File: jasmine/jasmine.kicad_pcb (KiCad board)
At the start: 2 copper layers, 70.7 x 53.3 mm, 27 parts, among them J1 NEIGHBOR1, J2 NEIGHBOR2, J3 USB-MICRO-B-SHIELDED, J4 LIPO_BATT_CONN, J7 BONUS_ROW, P1 TEST_POINT, P2 TEST_POINT, P3 TEST_POINT, P5 3.7_VDC, U1 MCP73831T

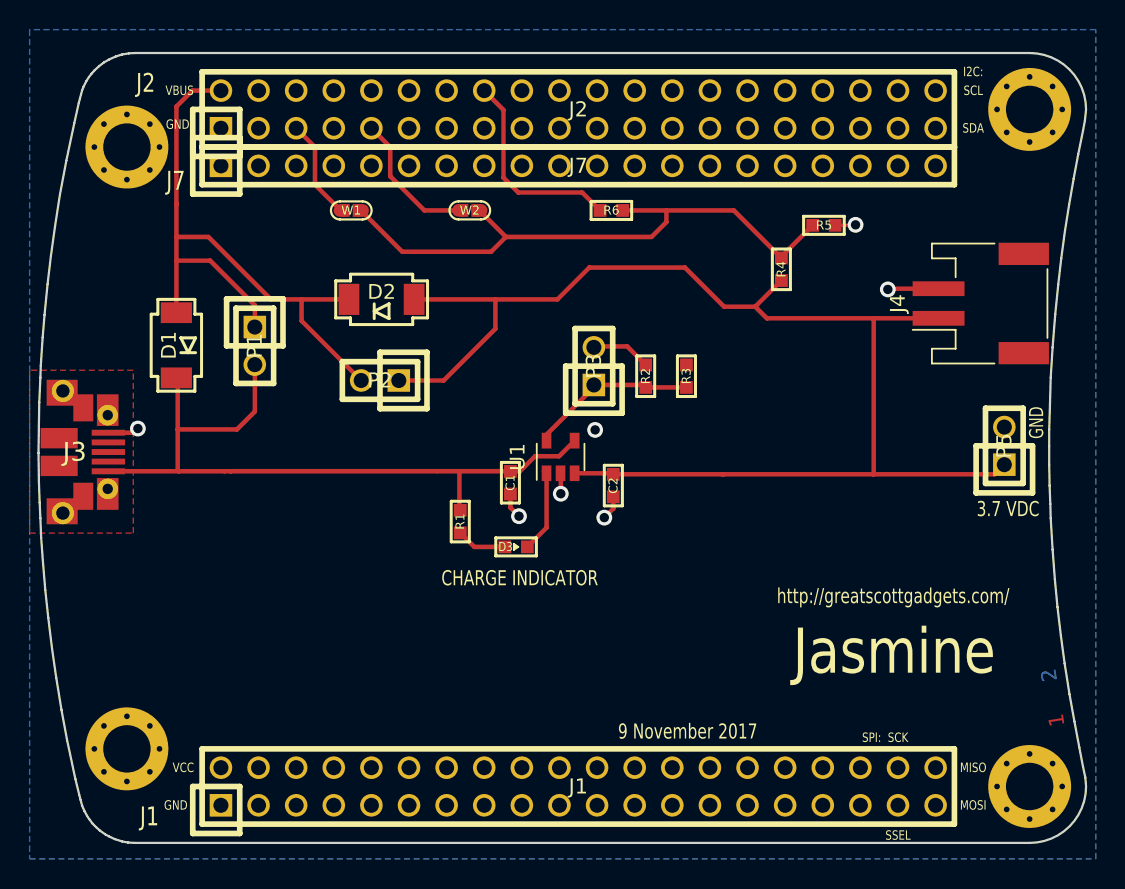
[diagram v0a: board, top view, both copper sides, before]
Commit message: JASMINE: Revised charge rate config; Added DNP JST connector; Added DNP screw terminal; Added load switch w/ LED indicator; Updated labeling on silkscreen LUCKY BAMBOO: updated soldermask clearance
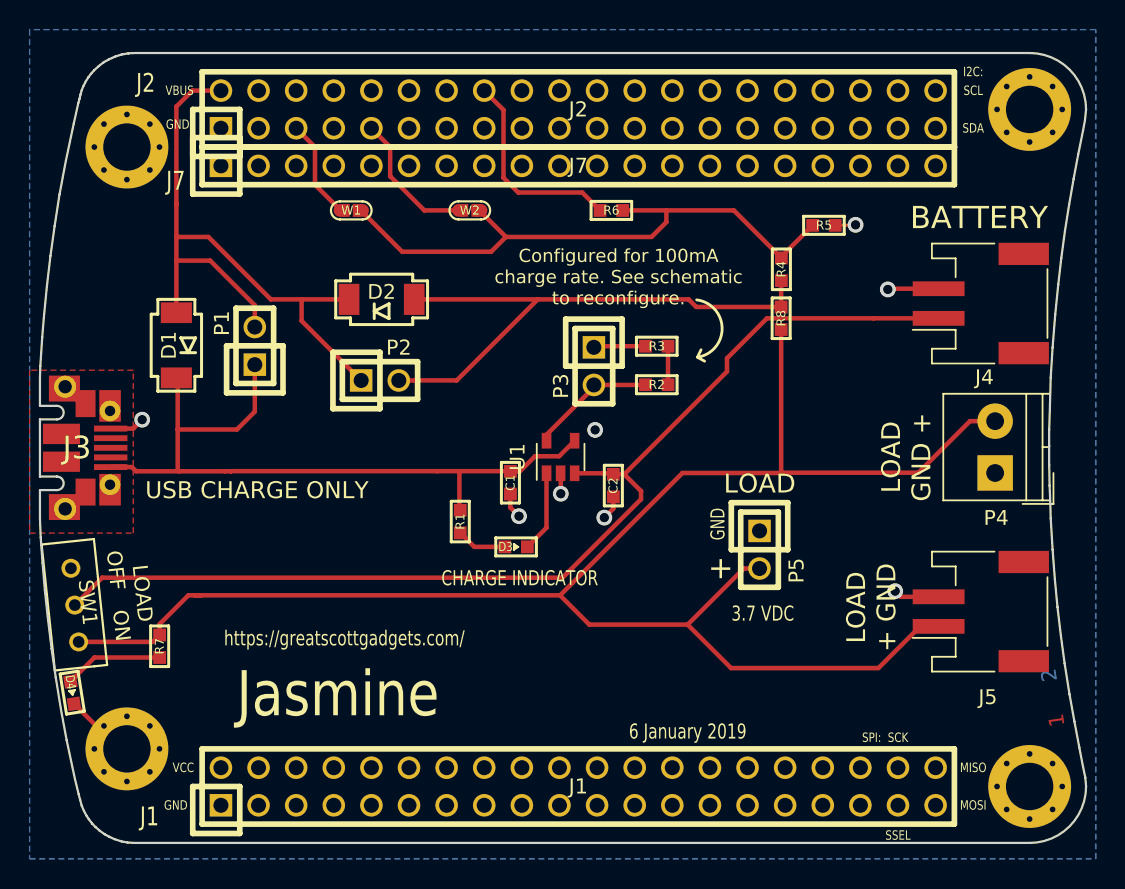
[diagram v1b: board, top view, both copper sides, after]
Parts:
- added D4: LED, gsg-modules:0603D, F.Cu at (111.9, 111.8)
- added J5: 2PIN_BATT_CONN, gsg-modules:JST_PH_S2B-PH-SM4-TB_02x2.00mm_Angled, F.Cu at (173.3, 106.3)
- added P4: 3.7_VDC, gsg-modules:TerminalBlock_4UCON_19963_02x3.5mm_Straight, F.Cu at (174.2, 96.9)
- added R7: 330, gsg-modules:0603, F.Cu at (117.8, 108.6)
- added R8: 0, gsg-modules:0603, F.Cu at (159.8, 86.5)
- added SW1: SW_SPDT, gsg-modules:MHSS1105, F.Cu at (112.0, 105.9)
- J4: footprint Connectors_JST:JST_PH_S2B-PH-SM4-TB_02x2.00mm_Angled -> gsg-modules:JST_PH_S2B-PH-SM4-TB_02x2.00mm_Angled
- R2: value 10k -> 7.5k
- moved P5 18.0 mm to (158.3, 102.1), turned to 270 degrees
- moved R3 2.85 mm to (151.3, 88.4), turned to 0 degrees
- moved R2 0.94 mm to (151.3, 91.0), turned to 180 degrees
- moved J3 0.32 mm to (109.7, 95.2)
- turned P1 to 90 degrees
- turned P2 to 0 degrees
- turned P3 to 270 degrees
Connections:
- D2 pad 2: Net-(C2-Pad2) -> Net-(D2-Pad2)
- P1 pad 1: /+5V -> Net-(C1-Pad2)
- P1 pad 2: Net-(C1-Pad2) -> /+5V
- P2 pad 1: Net-(C2-Pad2) -> /+5V
- P2 pad 2: /+5V -> Net-(D2-Pad2)
- P3 pad 1: Net-(P3-Pad1) -> GND
- P3 pad 2: GND -> Net-(P3-Pad2)
- P5 pad 1: Net-(C2-Pad2) -> GND
- P5 pad 2: GND -> Net-(J5-Pad1)
- R2 pad 1: GND -> Net-(R2-Pad1)
- R2 pad 2: Net-(P3-Pad1) -> Net-(P3-Pad2)
- R3 pad 2: Net-(P3-Pad1) -> Net-(R2-Pad1)
- R4 pad 1: Net-(C2-Pad2) -> Net-(D2-Pad2)
- U1 pad 5: Net-(P3-Pad1) -> Net-(P3-Pad2)
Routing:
- net Net-(J5-Pad1): track 0.00 -> 114.1 mm
- net Net-(D2-Pad2): track 0.00 -> 38.4 mm
- net Net-(C2-Pad2): track 90.5 -> 73.2 mm
- net Net-(P3-Pad1): track 11.4 -> 0.00 mm
- net GND: track 15.7 -> 24.3 mm, vias 6 -> 7
- net Net-(P3-Pad2): track 0.00 -> 8.58 mm
- net Net-(D4-Pad2): track 0.00 -> 6.69 mm
- net Net-(R2-Pad1): track 0.00 -> 2.60 mm
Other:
- board size 70.7 x 53.3 mm -> 70.6 x 53.3 mm
- board text added: "+"
- board text added: "6 January 2019"
- board text added: "BATTERY"
- board text added: "Configured for 100mA charge rate. See schematic to reconfigure."
- board text added: "LOAD"
- board text added: "LOAD + GND"
- board text added: "LOAD GND +"
- board text added: "LOAD OFF ON"
- board text added: "USB CHARGE ONLY"
- board text added: "https://greatscottgadgets.com/"
- board text removed: "9 November 2017"
- board text removed: "http://greatscottgadgets.com/"

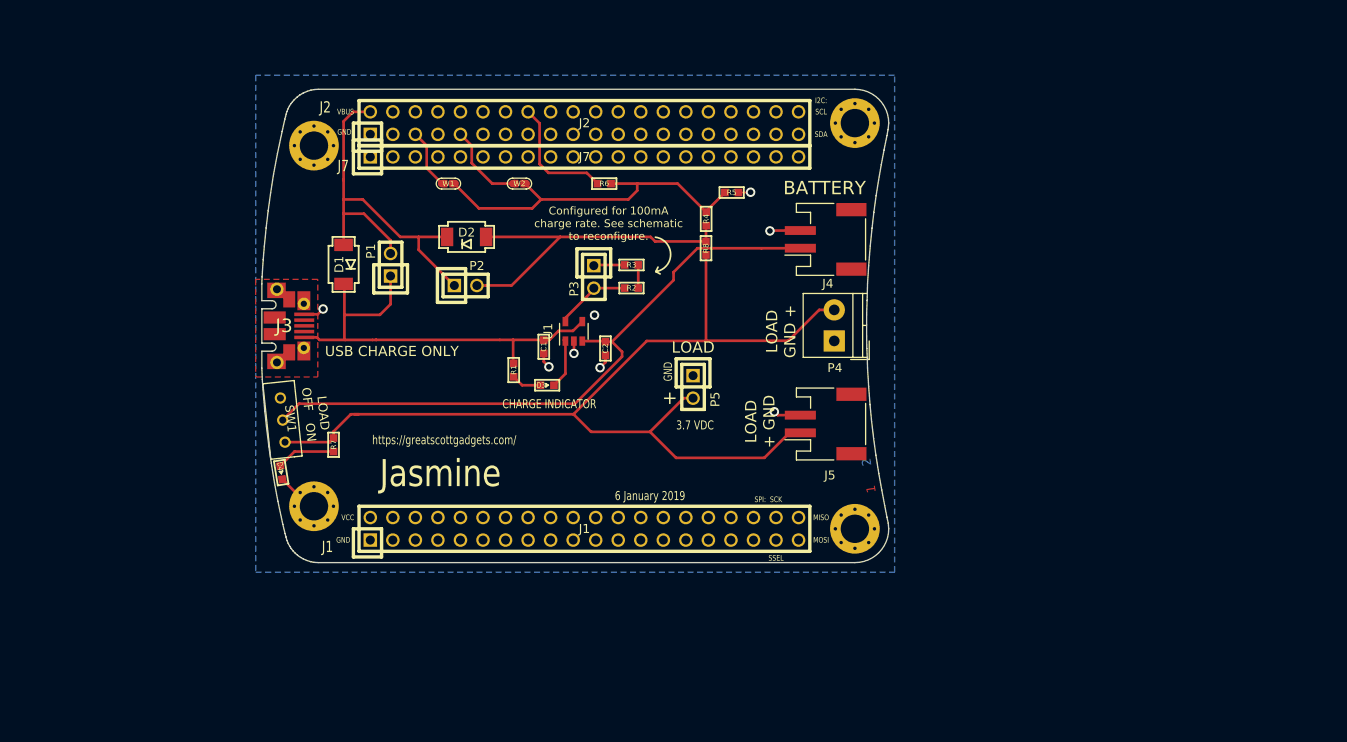
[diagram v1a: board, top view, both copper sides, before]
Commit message: Cleaned up jasmine.sch; Started Jasmine layout
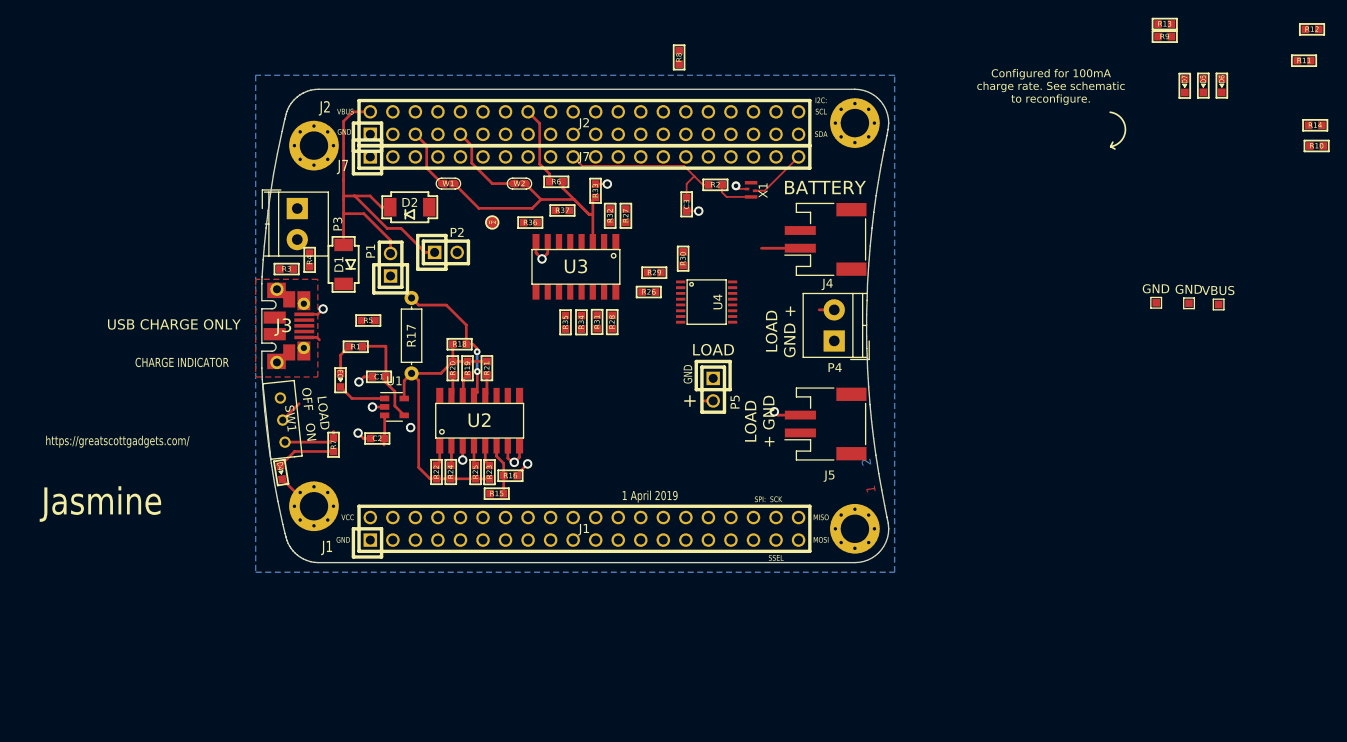
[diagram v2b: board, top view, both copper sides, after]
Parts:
- added C3: C, gsg-modules:0603, F.Cu at (157.6, 81.5)
- added D5: LED, gsg-modules:0603D, F.Cu at (215.8, 68.2)
- added D6: LED, gsg-modules:0603D, F.Cu at (217.9, 68.2)
- added D7: LED, gsg-modules:0603D, F.Cu at (213.7, 68.2)
- added GND: , gsg-modules:1Pin_0603, F.Cu at (210.5, 92.6)
- added GND: , gsg-modules:1Pin_0603, F.Cu at (214.2, 92.7)
- added R10: 330, gsg-modules:0603, F.Cu at (228.6, 75.0)
- added R11: 10k, gsg-modules:0603, F.Cu at (227.1, 65.4)
- added R12: 330, gsg-modules:0603, F.Cu at (228.0, 61.8)
- added R13: 10k, gsg-modules:0603, F.Cu at (211.4, 61.2)
- added R14: 10k, gsg-modules:0603, F.Cu at (228.4, 72.6)
- added R15: 10k, gsg-modules:0603, F.Cu at (136.2, 114.2)
- added R16: 10k, gsg-modules:0603, F.Cu at (137.7, 112.1)
- added R17: R, gsg-modules:RESISTOR-AXIAL-2.3x6.0mm, F.Cu at (126.6, 96.3)
- added R18: 67k, gsg-modules:0603, F.Cu at (132.0, 97.3)
- added R19: 2k, gsg-modules:0603, F.Cu at (132.9, 100.0)
- added R20: 2.5k, gsg-modules:0603, F.Cu at (131.2, 100.0)
- added R21: 3.33k, gsg-modules:0603, F.Cu at (135.1, 100.0)
- added R22: 5k, gsg-modules:0603, F.Cu at (129.4, 111.7)
- added R23: 10k, gsg-modules:0603, F.Cu at (135.3, 111.7)
- added R24: 25k, gsg-modules:0603, F.Cu at (131.0, 111.7)
- added R25: 67k, gsg-modules:0603, F.Cu at (133.8, 111.7)
- added R26: 10k, gsg-modules:0603, F.Cu at (153.3, 91.4)
- added R27: 0, gsg-modules:0603, F.Cu at (150.7, 82.8)
- added R28: 100k, gsg-modules:0603, F.Cu at (149.2, 94.8)
- added R29: 10k, gsg-modules:0603, F.Cu at (153.9, 89.2)
- added R30: 10k, gsg-modules:0603, F.Cu at (157.2, 87.7)
- added R31: 100k, gsg-modules:0603, F.Cu at (147.5, 94.8)
- added R32: 100k, gsg-modules:0603, F.Cu at (148.9, 82.8)
- added R33: 100k, gsg-modules:0603, F.Cu at (147.3, 80.0)
- added R34: 100k, gsg-modules:0603, F.Cu at (145.7, 94.8)
- added R35: 100k, gsg-modules:0603, F.Cu at (143.9, 94.8)
- added R36: 100k, gsg-modules:0603, F.Cu at (139.9, 83.6)
- added R37: 100k, gsg-modules:0603, F.Cu at (143.6, 82.2)
- added R9: 330, gsg-modules:0603, F.Cu at (211.4, 62.7)
- added TP4: TestPoint, gsg-modules:TESTPOINT-50MIL, F.Cu at (135.7, 83.6)
- added U2: 74HC4051, gsg-modules:SOIC16, F.Cu at (134.2, 105.9)
- added U3: 74HC4051, gsg-modules:SOIC16, F.Cu at (145.1, 88.6)
- added U4: PCA9674, gsg-modules:TSSOP16, F.Cu at (159.8, 92.6)
- added VBUS: , gsg-modules:1Pin_0603, F.Cu at (217.5, 92.8)
- added X1: SiT1533, gsg-modules:SiT1533, F.Cu at (164.8, 79.9)
- P3: value TEST_POINT -> INPUT; footprint gsg-modules:HEADER-1x2 -> gsg-modules:TerminalBlock_4UCON_19963_02x3.5mm_Straight
- R2: value 7.5k -> 0
- R3: value 2.5k -> DNP
- R4: value 100k -> 0
- R5: value 100k -> 0.1
- moved R4 44.9 mm to (115.1, 87.8)
- moved R5 43.4 mm to (121.7, 94.6), turned to 180 degrees
- moved R3 38.9 mm to (112.5, 88.8)
- moved P3 34.3 mm to (113.7, 82.0)
- moved C2 27.6 mm to (122.7, 107.9), turned to 0 degrees
- moved D3 23.3 mm to (118.6, 101.4), turned to 90 degrees
- moved U1 21.9 mm to (124.6, 104.4), turned to 0 degrees
- moved R8 21.7 mm to (156.7, 65.0)
- moved C1 18.9 mm to (122.9, 101.0), turned to 0 degrees
- moved R1 18.0 mm to (120.3, 97.6), turned to 180 degrees
- moved R2 15.0 mm to (160.8, 79.3)
- moved D2 7.22 mm to (126.4, 81.9)
- moved R6 5.41 mm to (142.9, 79.0)
- moved P2 4.34 mm to (130.4, 87.0)
- moved P5 2.29 mm to (160.6, 102.4)
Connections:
- C1 pad 2: Net-(C1-Pad2) -> /STAT_i
- C2 pad 2: Net-(C2-Pad2) -> /BATT_i
- D1 pad 1: Net-(C1-Pad2) -> /VBUS_i
- J1 pad 2: Net-(J1-Pad2) -> VCC
- J3 pad 1: Net-(C1-Pad2) -> /VBUS_i
- J4 pad 1: Net-(C2-Pad2) -> GND
- J4 pad 2: GND -> /BATT_i
- J5 pad 1: Net-(J5-Pad1) -> GND
- J5 pad 2: GND -> /VBAT
- J7 pad 10: GND -> /RTCX1
- J7 pad 20: Net-(J7-Pad20) -> VCC
- P1 pad 1: Net-(C1-Pad2) -> /VBUS_i
- P4 pad 2: Net-(J5-Pad1) -> /VBAT
- P5 pad 1: GND -> /VBAT
- P5 pad 2: Net-(J5-Pad1) -> GND
- R1 pad 1: Net-(C1-Pad2) -> /STAT_i
- R2 pad 2: Net-(P3-Pad2) -> /RTCX1
- R3 pad 1: GND -> /VBUS_i
- R3 pad 2: Net-(R2-Pad1) -> GND
- R4 pad 1: Net-(D2-Pad2) -> Net-(P3-Pad2)
- R4 pad 2: Net-(R4-Pad2) -> /VBUS_i
- R5 pad 1: Net-(R4-Pad2) -> /STAT_i
- R5 pad 2: GND -> /VBUS_i
- R6 pad 1: Net-(R4-Pad2) -> Net-(R33-Pad2)
- R7 pad 1: Net-(J5-Pad1) -> /VBAT
- R8 pad 1: Net-(J5-Pad1) -> /VBAT
- SW1 pad 1: Net-(J5-Pad1) -> /VBAT
- SW1 pad 2: Net-(C2-Pad2) -> /BATT_i
- U1 pad 3: Net-(C2-Pad2) -> /BATT_i
- U1 pad 4: Net-(C1-Pad2) -> /STAT_i
- U1 pad 5: Net-(P3-Pad2) -> /PROG_i
- W1 pad 2: Net-(R4-Pad2) -> Net-(R33-Pad2)
- W2 pad 2: Net-(R4-Pad2) -> Net-(R33-Pad2)
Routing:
- net Net-(J5-Pad1): track 114.1 -> 0.00 mm
- net Net-(C2-Pad2): track 73.2 -> 0.00 mm
- net Net-(C1-Pad2): track 50.5 -> 0.00 mm
- net Net-(R4-Pad2): track 41.1 -> 0.00 mm
- net Net-(D2-Pad2): track 38.4 -> 0.00 mm
- net /PROG_i: track 0.00 -> 34.0 mm
- net Net-(R33-Pad2): track 0.00 -> 30.5 mm
- net /RTCX1: track 0.00 -> 19.3 mm
- net Net-(R17-Pad1): track 0.00 -> 16.5 mm, vias 0 -> 2
- net GND: track 24.3 -> 36.0 mm, vias 7 -> 11
- net /VBAT: track 0.00 -> 11.4 mm, vias 0 -> 1
- net /STAT_i: track 0.00 -> 11.3 mm
- net Net-(P3-Pad2): track 8.58 -> 0.02 mm, vias 0 -> 1
- net VCC: track 0.00 -> 6.48 mm
- net /BATT_i: track 0.00 -> 6.30 mm
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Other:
- board text added: "1 April 2019"
- board text removed: "3.7 VDC"
- board text removed: "6 January 2019"

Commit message: Updates to jasmine schematic and layout; Updated neighbor-template to be compatible with KiCAD 5.1.2
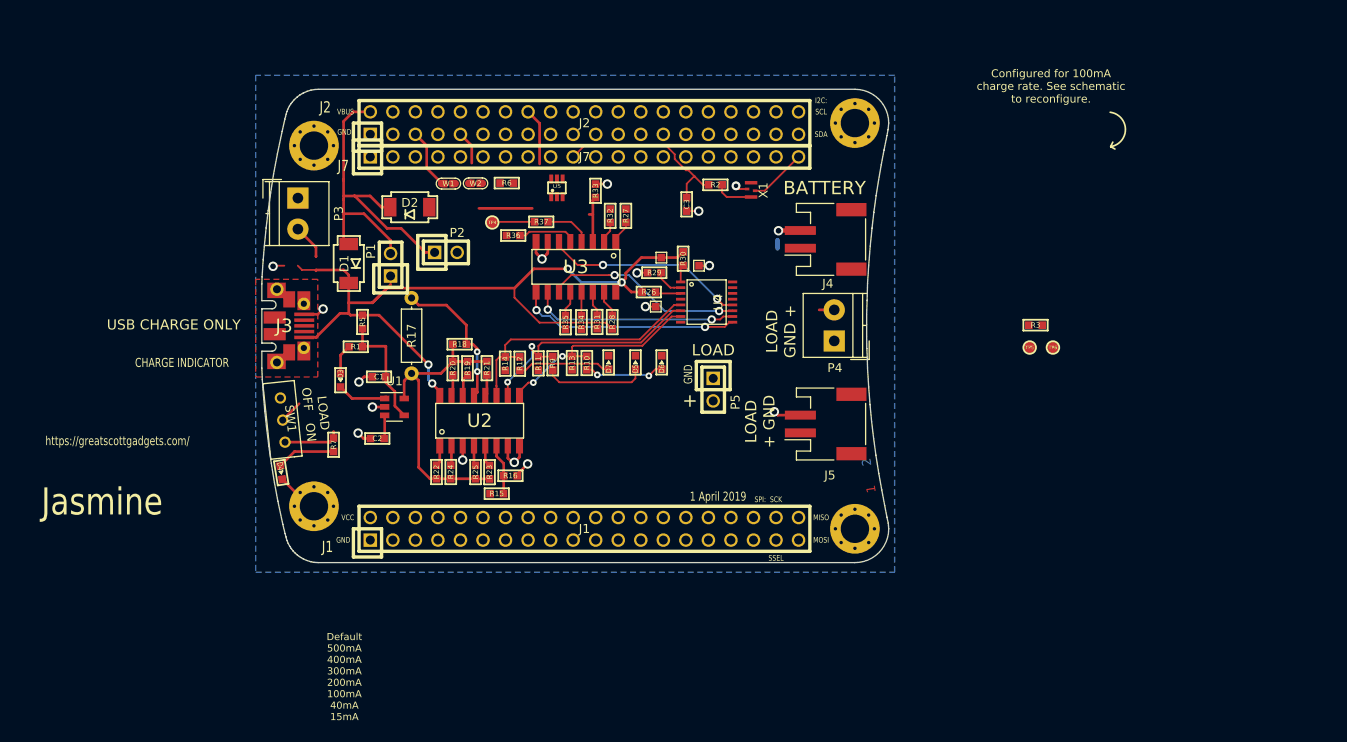
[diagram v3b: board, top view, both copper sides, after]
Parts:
- removed GND (x2): , gsg-modules:1Pin_0603
- removed R4, R8: 0, gsg-modules:0603
- added TP1: , gsg-modules:1Pin_0603, F.Cu at (159.0, 88.5)
- added TP2: , gsg-modules:1Pin_0603, F.Cu at (154.1, 93.1)
- added TP5: TestPoint, gsg-modules:TESTPOINT-50MIL, F.Cu at (196.2, 97.7)
- added TP6: TestPoint, gsg-modules:TESTPOINT-50MIL, F.Cu at (198.8, 97.7)
- added U5: 74LVC1G3157, gsg-modules:SOT363, F.Cu at (142.9, 79.7)
- R3: value DNP -> 10k
- moved R12 96.9 mm to (138.8, 99.5), turned to 270 degrees
- moved R14 95.1 mm to (137.1, 99.5), turned to 270 degrees
- moved R11 92.8 mm to (140.9, 99.5), turned to 90 degrees
- moved R10 85.8 mm to (146.3, 99.4), turned to 270 degrees
- moved R3 84.6 mm to (196.9, 95.2)
- moved R9 78.2 mm to (142.5, 99.5), turned to 270 degrees
- moved R13 76.9 mm to (144.7, 99.4), turned to 90 degrees
- moved D7 72.0 mm to (148.8, 99.4), turned to 270 degrees
- moved D5 71.2 mm to (151.8, 99.4), turned to 270 degrees
- moved D6 70.4 mm to (154.8, 99.4), turned to 270 degrees
- moved TP3 63.0 mm to (154.7, 87.5)
- moved R6 5.58 mm to (137.3, 79.2), turned to 0 degrees
- moved W2 4.94 mm to (133.8, 79.2)
- moved R37 2.71 mm to (141.2, 83.5)
- moved R36 2.41 mm to (138.0, 85.1)
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- renumbered VBUS to TP3
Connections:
- net /PROG_i renamed /PROG
- C1 pad 2: /STAT_i -> /VIN
- C2 pad 2: /BATT_i -> /BATT
- D1 pad 1: /VBUS_i -> VBUS
- D2 pad 2: Net-(D2-Pad2) -> /VBAT
- D3 pad 1: Net-(D3-Pad1) -> /STAT
- J3 pad 1: /VBUS_i -> VBUS
- J4 pad 1: GND -> /BATT
- J4 pad 2: /BATT_i -> GND
- J5 pad 1: GND -> /VBAT
- J5 pad 2: /VBAT -> GND
- P1 pad 1: /VBUS_i -> VBUS
- P2 pad 2: Net-(D2-Pad2) -> /VBAT
- P3 pad 2: Net-(P3-Pad2) -> VBUS
- R1 pad 1: /STAT_i -> /VIN
- R28 pad 1: /VBUS_i -> VBUS
- R3 pad 1: /VBUS_i -> /MEASURE_E
- R3 pad 2: GND -> VCC
- R31 pad 1: /STAT_i -> /VIN
- R32 pad 1: /STAT_i -> /STAT
- R34 pad 1: /BATT_i -> /BATT
- R35 pad 2: /LOAD_i -> /BATT
- R5 pad 1: /STAT_i -> /VIN
- R5 pad 2: /VBUS_i -> VBUS
- R6 pad 1: Net-(R33-Pad2) -> Net-(R6-Pad1)
- SW1 pad 2: /BATT_i -> /BATT
- U1 pad 1: Net-(D3-Pad1) -> /STAT
- U1 pad 3: /BATT_i -> /BATT
- U1 pad 4: /STAT_i -> /VIN
- W1 pad 2: Net-(R33-Pad2) -> Net-(R6-Pad1)
- W2 pad 2: Net-(R33-Pad2) -> Net-(R6-Pad1)
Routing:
- net VBUS: track 0.00 -> 99.4 mm, vias 0 -> 4
- net /RATE_S0: track 0.00 -> 29.8 mm
- net /RATE_S1: track 0.00 -> 28.7 mm, vias 0 -> 2
- net /MEASURE_S2: track 0.00 -> 25.2 mm, vias 0 -> 2
- net /RATE_S2: track 0.00 -> 24.4 mm, vias 0 -> 2
- net /MEASURE_S1: track 0.00 -> 23.4 mm, vias 0 -> 2
- net /MEASURE_E: track 0.00 -> 22.8 mm, vias 0 -> 2
- net /MEASURE_S0: track 0.00 -> 22.3 mm, vias 0 -> 2
- net Net-(R33-Pad2): track 30.5 -> 11.5 mm
- net /VIN: track 0.00 -> 13.3 mm
- net Net-(D5-Pad2): track 0.00 -> 11.5 mm
- net /STAT_i: track 11.3 -> 0.00 mm
- net Net-(D7-Pad2): track 0.00 -> 10.6 mm
- net Net-(D6-Pad2): track 0.00 -> 9.05 mm, vias 0 -> 2
- net Net-(R36-Pad2): track 0.00 -> 7.17 mm
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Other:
- board text added: "Default 500mA 400mA 300mA 200mA 100mA 40mA 15mA"
